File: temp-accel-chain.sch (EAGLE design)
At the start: 10 parts, among them U1 ADT7420UCPZ-R2, U2 ADXL345

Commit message: renumbered
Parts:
- JP1, JP2: value (none) -> JUMPER-3SMD; device jumper:JP3Q -> SparkFun-Passives:JUMPER-3SMD
- JP4, JP5: value JUMPER-3SMD -> (none); device SparkFun-Passives:JUMPER-3SMD -> jumper:JP3Q
- renumbered R2 to R1
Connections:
- net ADD_SEL: now also JP1.2; no longer JP5.2
- net GND: now also JP4.1; no longer JP2.1
- net SCL: now also JP3.2; no longer JP4.2
- net SCL1: now also JP3.3, JP4.5, JP5.5; no longer JP1.5, JP2.5, JP4.3
- net SCL2: now also JP3.1, JP4.3, JP5.3; no longer JP1.3, JP2.3, JP4.1
- net SDA: now also JP2.2; no longer JP3.2
- net SDA1: now also JP2.3, JP4.6, JP5.6; no longer JP1.6, JP2.6, JP3.3
- net SDA2: now also JP2.1, JP4.4, JP5.4; no longer JP1.4, JP2.4, JP3.1
- net VCC: now also JP1.3, JP4.2, JP5.2; no longer JP1.2, JP2.2, JP5.3
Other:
- moved on the sheet: JP3
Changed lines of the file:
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@@
 </classes>
 <parts>
-<part name="JP1" library="jumper" deviceset="JP3Q" device=""/>
-<part name="JP2" library="jumper" deviceset="JP3Q" device=""/>
+<part name="JP5" library="jumper" deviceset="JP3Q" device=""/>
+<part name="JP4" library="jumper" deviceset="JP3Q" device=""/>
+<part name="JP2" library="SparkFun-Passives" deviceset="JUMPER-3" device="SMD"/>
 <part name="JP3" library="SparkFun-Passives" deviceset="JUMPER-3" device="SMD"/>
-<part name="JP4" library="SparkFun-Passives" deviceset="JUMPER-3" device="SMD"/>
 <part name="C1" library="resistor" deviceset="C-EU" device="C0805"/>
 <part name="GND1" library="supply1" deviceset="GND" device=""/>
@@
 <part name="U1" library="farnell-parts" deviceset="ADT7420UCPZ-R2" device=""/>
 <part name="GND3" library="supply1" deviceset="GND" device=""/>
-<part name="JP5" library="SparkFun-Passives" deviceset="JUMPER-3" device="SMD"/>
+<part name="JP1" library="SparkFun-Passives" deviceset="JUMPER-3" device="SMD"/>
 <part name="GND4" library="supply1" deviceset="GND" device=""/>
-<part name="R2" library="resistor" deviceset="R-EU_" device="R0603" value="10K"/>
+<part name="R1" library="resistor" deviceset="R-EU_" device="R0603" value="10K"/>
 <part name="FRAME1" library="frames" deviceset="A4L-LOC" device=""/>
 <part name="U2" library="SparkFun-Sensors" deviceset="ADXL345" device=""/>
@@
 </plain>
 <instances>
-<instance part="JP1" gate="B" x="73.66" y="38.1" rot="R90"/>
-<instance part="JP2" gate="B" x="73.66" y="58.42" rot="R90"/>
-<instance part="JP3" gate="G$1" x="60.96" y="99.06" rot="R90"/>
-<instance part="JP4" gate="G$1" x="60.96" y="83.82" rot="R90"/>
+<instance part="JP5" gate="B" x="73.66" y="38.1" rot="R90"/>
+<instance part="JP4" gate="B" x="73.66" y="58.42" rot="R90"/>
+<instance part="JP2" gate="G$1" x="60.96" y="99.06" rot="R90"/>
+<instance part="JP3" gate="G$1" x="60.96" y="83.82" rot="R90"/>
 <instance part="C1" gate="G$1" x="121.92" y="43.18"/>
 <instance part="GND1" gate="1" x="88.9" y="33.02"/>
@@
 <instance part="U1" gate="A" x="152.4" y="99.06"/>
 <instance part="GND3" gate="1" x="119.38" y="83.82"/>
-<instance part="JP5" gate="G$1" x="60.96" y="114.3" rot="R90"/>
+<instance part="JP1" gate="G$1" x="60.96" y="114.3" rot="R90"/>
 <instance part="GND4" gate="1" x="63.5" y="111.76"/>
-<instance part="R2" gate="G$1" x="119.38" y="101.6"/>
+<instance part="R1" gate="G$1" x="119.38" y="101.6"/>
 <instance part="FRAME1" gate="G$1" x="0" y="0"/>
 <instance part="U2" gate="G$1" x="203.2" y="142.24"/>
@@
 <net name="SDA1" class="0">
 <segment>
-<pinref part="JP2" gate="B" pin="6"/>
+<pinref part="JP4" gate="B" pin="6"/>
 <wire x1="66.04" y1="60.96" x2="58.42" y2="60.96" width="0.1524" layer="91"/>
 <wire x1="58.42" y1="60.96" x2="58.42" y2="40.64" width="0.1524" layer="91"/>
-<pinref part="JP1" gate="B" pin="6"/>
+<pinref part="JP5" gate="B" pin="6"/>
 <wire x1="58.42" y1="40.64" x2="66.04" y2="40.64" width="0.1524" layer="91"/>
 <label x="58.42" y="60.96" size="1.778" layer="95"/>
 </segment>
 <segment>
-<pinref part="JP3" gate="G$1" pin="3"/>
+<pinref part="JP2" gate="G$1" pin="3"/>
 <wire x1="63.5" y1="104.14" x2="78.74" y2="104.14" width="0.1524" layer="91"/>
 <label x="73.66" y="104.14" size="1.778" layer="95"/>
@@
 <net name="SDA2" class="0">
 <segment>
-<pinref part="JP2" gate="B" pin="4"/>
+<pinref part="JP4" gate="B" pin="4"/>
 <wire x1="66.04" y1="58.42" x2="55.88" y2="58.42" width="0.1524" layer="91"/>
 <wire x1="55.88" y1="58.42" x2="55.88" y2="38.1" width="0.1524" layer="91"/>
-<pinref part="JP1" gate="B" pin="4"/>
+<pinref part="JP5" gate="B" pin="4"/>
 <wire x1="55.88" y1="38.1" x2="66.04" y2="38.1" width="0.1524" layer="91"/>
 <label x="58.42" y="58.42" size="1.778" layer="95"/>
 </segment>
 <segment>
-<pinref part="JP3" gate="G$1" pin="1"/>
+<pinref part="JP2" gate="G$1" pin="1"/>
 <wire x1="63.5" y1="99.06" x2="78.74" y2="99.06" width="0.1524" layer="91"/>
 <label x="73.66" y="99.06" size="1.778" layer="95"/>
@@
 <net name="VCC" class="0">
 <segment>
-<pinref part="JP2" gate="B" pin="2"/>
+<pinref part="JP4" gate="B" pin="2"/>
 <wire x1="66.04" y1="55.88" x2="53.34" y2="55.88" width="0.1524" layer="91"/>
 <wire x1="53.34" y1="55.88" x2="53.34" y2="35.56" width="0.1524" layer="91"/>
-<pinref part="JP1" gate="B" pin="2"/>
+<pinref part="JP5" gate="B" pin="2"/>
 <wire x1="53.34" y1="35.56" x2="66.04" y2="35.56" width="0.1524" layer="91"/>
 <label x="58.42" y="55.88" size="1.778" layer="95"/>
@@
 </segment>
 <segment>
-<pinref part="JP5" gate="G$1" pin="3"/>
+<pinref part="JP1" gate="G$1" pin="3"/>
 <wire x1="63.5" y1="119.38" x2="76.2" y2="119.38" width="0.1524" layer="91"/>
 <label x="71.12" y="119.38" size="1.778" layer="95"/>
@@
 <net name="SCL1" class="0">
 <segment>
-<pinref part="JP2" gate="B" pin="5"/>
+<pinref part="JP4" gate="B" pin="5"/>
 <wire x1="81.28" y1="60.96" x2="91.44" y2="60.96" width="0.1524" layer="91"/>
 <wire x1="91.44" y1="60.96" x2="91.44" y2="40.64" width="0.1524" layer="91"/>
-<pinref part="JP1" gate="B" pin="5"/>
+<pinref part="JP5" gate="B" pin="5"/>
 <wire x1="91.44" y1="40.64" x2="81.28" y2="40.64" width="0.1524" layer="91"/>
 <label x="83.82" y="60.96" size="1.778" layer="95"/>
 </segment>
 <segment>
-<pinref part="JP4" gate="G$1" pin="3"/>
+<pinref part="JP3" gate="G$1" pin="3"/>
 <wire x1="63.5" y1="88.9" x2="78.74" y2="88.9" width="0.1524" layer="91"/>
 <label x="73.66" y="88.9" size="1.778" layer="95"/>
@@
 <net name="SCL2" class="0">
 <segment>
-<pinref part="JP2" gate="B" pin="3"/>
+<pinref part="JP4" gate="B" pin="3"/>
 <wire x1="81.28" y1="58.42" x2="93.98" y2="58.42" width="0.1524" layer="91"/>
 <wire x1="93.98" y1="58.42" x2="93.98" y2="38.1" width="0.1524" layer="91"/>
-<pinref part="JP1" gate="B" pin="3"/>
+<pinref part="JP5" gate="B" pin="3"/>
 <wire x1="93.98" y1="38.1" x2="81.28" y2="38.1" width="0.1524" layer="91"/>
 <label x="83.82" y="58.42" size="1.778" layer="95"/>
 </segment>
 <segment>
-<pinref part="JP4" gate="G$1" pin="1"/>
+<pinref part="JP3" gate="G$1" pin="1"/>
 <wire x1="63.5" y1="83.82" x2="78.74" y2="83.82" width="0.1524" layer="91"/>
 <label x="73.66" y="83.82" size="1.778" layer="95"/>
@@
 <net name="GND" class="0">
 <segment>
-<pinref part="JP2" gate="B" pin="1"/>
+<pinref part="JP4" gate="B" pin="1"/>
 <wire x1="81.28" y1="55.88" x2="96.52" y2="55.88" width="0.1524" layer="91"/>
 <wire x1="96.52" y1="55.88" x2="96.52" y2="35.56" width="0.1524" layer="91"/>
-<pinref part="JP1" gate="B" pin="1"/>
+<pinref part="JP5" gate="B" pin="1"/>
 <wire x1="96.52" y1="35.56" x2="88.9" y2="35.56" width="0.1524" layer="91"/>
 <label x="83.82" y="55.88" size="1.778" layer="95"/>
@@
 </segment>
 <segment>
-<pinref part="JP5" gate="G$1" pin="1"/>
+<pinref part="JP1" gate="G$1" pin="1"/>
 <pinref part="GND4" gate="1" pin="GND"/>
 </segment>
@@
 <net name="SDA" class="0">
 <segment>
-<pinref part="JP3" gate="G$1" pin="2"/>
+<pinref part="JP2" gate="G$1" pin="2"/>
 <wire x1="63.5" y1="101.6" x2="78.74" y2="101.6" width="0.1524" layer="91"/>
 <label x="73.66" y="101.6" size="1.778" layer="95"/>
@@
 <net name="SCL" class="0">
 <segment>
-<pinref part="JP4" gate="G$1" pin="2"/>
+<pinref part="JP3" gate="G$1" pin="2"/>
 <wire x1="63.5" y1="86.36" x2="78.74" y2="86.36" width="0.1524" layer="91"/>
 <label x="73.66" y="86.36" size="1.778" layer="95"/>
@@
 <net name="ADD" class="0">
 <segment>
-<pinref part="R2" gate="G$1" pin="2"/>
+<pinref part="R1" gate="G$1" pin="2"/>
 <pinref part="U1" gate="A" pin="A1"/>
 <wire x1="124.46" y1="101.6" x2="134.62" y2="101.6" width="0.1524" layer="91"/>
@@
 <net name="ADD_SEL" class="0">
 <segment>
-<pinref part="R2" gate="G$1" pin="1"/>
+<pinref part="R1" gate="G$1" pin="1"/>
 <wire x1="114.3" y1="101.6" x2="104.14" y2="101.6" width="0.1524" layer="91"/>
 <label x="104.14" y="101.6" size="1.778" layer="95"/>
 </segment>
 <segment>
-<pinref part="JP5" gate="G$1" pin="2"/>
+<pinref part="JP1" gate="G$1" pin="2"/>
 <wire x1="63.5" y1="116.84" x2="76.2" y2="116.84" width="0.1524" layer="91"/>
 <label x="71.12" y="116.84" size="1.778" layer="95"/>

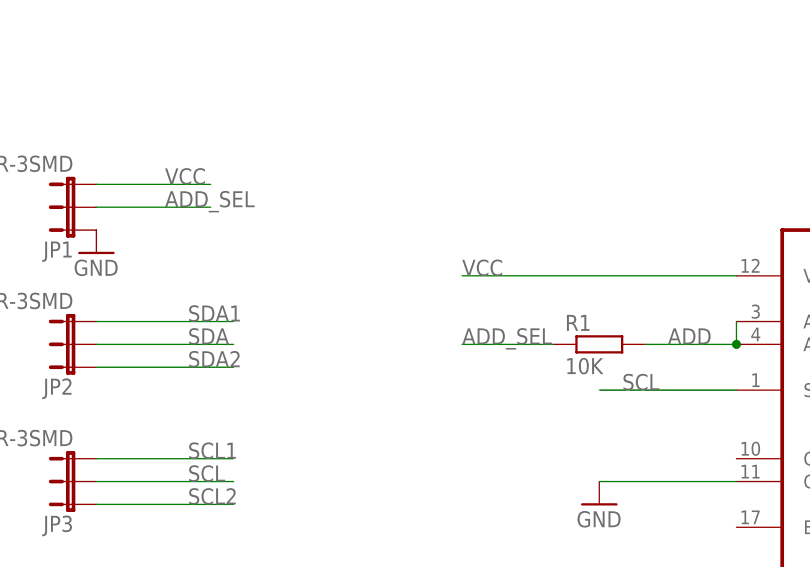
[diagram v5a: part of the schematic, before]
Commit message: removed unneeded resistor on add select pins
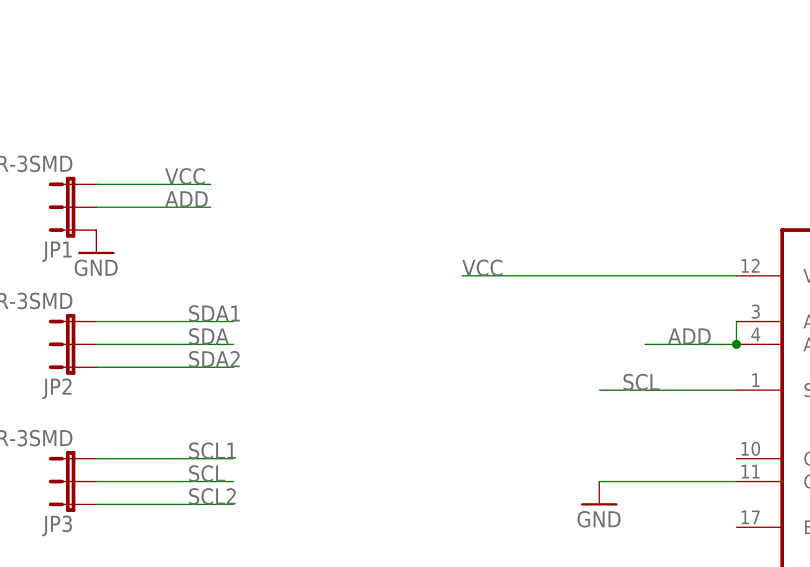
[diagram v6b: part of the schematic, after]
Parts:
- removed R1: 10K, resistor:R-EU_R0603
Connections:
- removed net ADD_SEL: JP1.2, R1.1
- net ADD: now also JP1.2; no longer R1.2
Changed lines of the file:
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@@
 <part name="JP1" library="SparkFun-Passives" deviceset="JUMPER-3" device="SMD"/>
 <part name="GND4" library="supply1" deviceset="GND" device=""/>
-<part name="R1" library="resistor" deviceset="R-EU_" device="R0603" value="10K"/>
 <part name="FRAME1" library="frames" deviceset="A4L-LOC" device=""/>
 <part name="U2" library="SparkFun-Sensors" deviceset="ADXL345" device=""/>
@@
 <instance part="JP1" gate="G$1" x="60.96" y="114.3" rot="R90"/>
 <instance part="GND4" gate="1" x="63.5" y="111.76"/>
-<instance part="R1" gate="G$1" x="119.38" y="101.6"/>
 <instance part="FRAME1" gate="G$1" x="0" y="0"/>
 <instance part="U2" gate="G$1" x="203.2" y="142.24"/>
@@
 <net name="ADD" class="0">
 <segment>
-<pinref part="R1" gate="G$1" pin="2"/>
 <pinref part="U1" gate="A" pin="A1"/>
 <wire x1="124.46" y1="101.6" x2="134.62" y2="101.6" width="0.1524" layer="91"/>
@@
 <label x="226.06" y="147.32" size="1.778" layer="95"/>
 </segment>
-</net>
-<net name="ADD_SEL" class="0">
-<segment>
-<pinref part="R1" gate="G$1" pin="1"/>
-<wire x1="114.3" y1="101.6" x2="104.14" y2="101.6" width="0.1524" layer="91"/>
-<label x="104.14" y="101.6" size="1.778" layer="95"/>
-</segment>
-<segment>
+<segment>
